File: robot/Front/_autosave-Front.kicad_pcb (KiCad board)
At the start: 2 copper layers, 40 x 40 mm, 42 parts, among them J1 USB_B_Micro, Q1 BC849, Q2 BC849, SW2 SW_Push, U1 CH340C, U10 ESP32-WROOM-32, U2 CJVL53L0XV2, U3 LD1117S33CTR

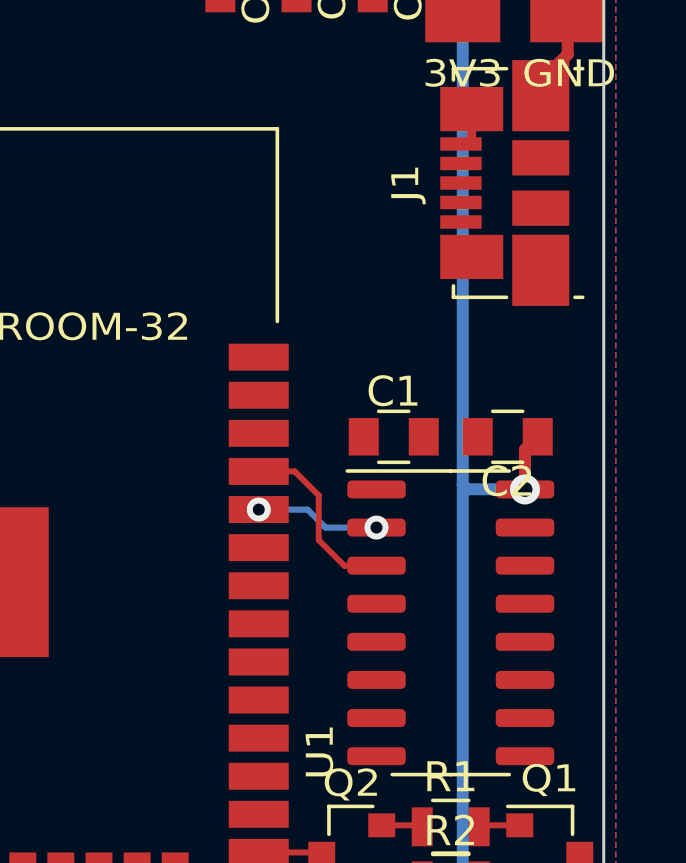
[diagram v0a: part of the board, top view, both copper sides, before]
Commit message: Shrink design
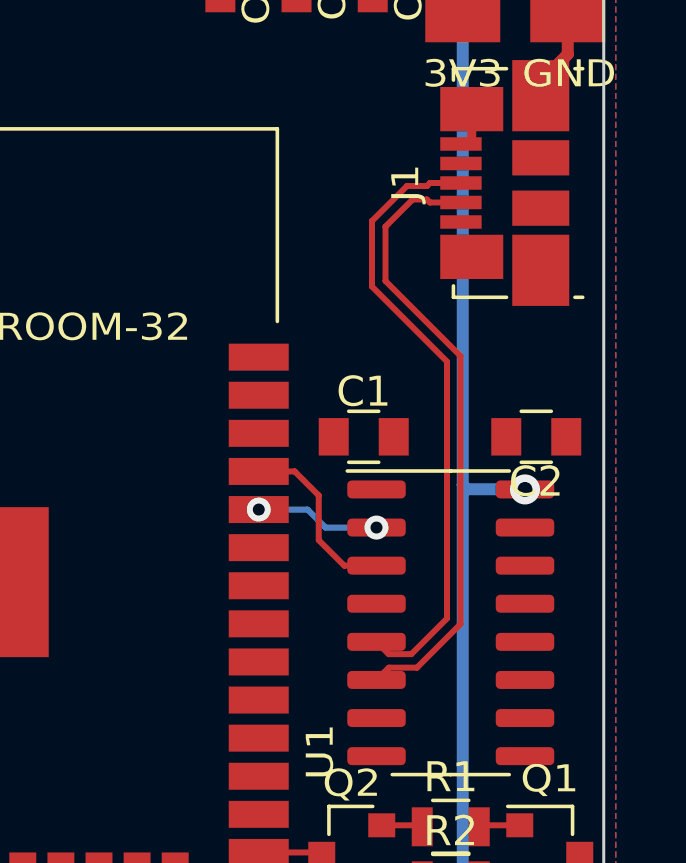
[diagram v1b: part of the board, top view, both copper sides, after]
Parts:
- moved C1 1.00 mm to (227.5, 121.1)
- moved C2 0.95 mm to (233.2, 121.1)
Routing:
- net /D-: track 0.00 -> 20.8 mm
- net /D+: track 0.00 -> 20.8 mm
- net +3V3: track 101.6 -> 99.7 mm
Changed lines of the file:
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@@
     (thickness 1.6)
     (drawings 7)
-    (tracks 131)
+    (tracks 149)
     (zones 0)
     (modules 42)
@@
   )
   (module Capacitors_SMD:C_0805 (layer F.Cu)
-    (at 228.5 121.1)
+    (at 227.5 121.1)
     (descr "Capacitor SMD 0805, reflow soldering, AVX (see smccp.pdf)")
     (tags "capacitor 0805")
@@
   )
   (module Capacitors_SMD:C_0805 (layer F.Cu)
-    (at 232.3 121.1 180)
+    (at 233.25 121.1 180)
     (descr "Capacitor SMD 0805, reflow soldering, AVX (see smccp.pdf)")
     (tags "capacitor 0805")
@@
   (via (at 230.8 140.55) (size 1) (drill 0.5) (layers F.Cu B.Cu) (net 4))
   (via (at 232.875 122.855) (size 1) (drill 0.5) (layers F.Cu B.Cu) (net 4))
-  (segment (start 232.875 121.525) (end 233.3 121.1) (width 0.4) (layer F.Cu) (net 4))
-  (segment (start 232.875 122.855) (end 232.875 121.525) (width 0.4) (layer F.Cu) (net 4))
   (segment (start 230.8 105.45) (end 230.8 122.7) (width 0.4) (layer B.Cu) (net 4))
   (segment (start 230.8 122.7) (end 230.8 140.55) (width 0.4) (layer B.Cu) (net 4))
@@
   (segment (start 204.525 136.88) (end 206.45 134.955) (width 0.4) (layer B.Cu) (net 35))
   (segment (start 201.64 136.88) (end 204.525 136.88) (width 0.4) (layer B.Cu) (net 35))
+  (segment (start 227.925 129.205) (end 228.335 128.795) (width 0.2) (layer F.Cu) (net 36))
+  (segment (start 228.335 128.795) (end 229.2732 128.795) (width 0.2) (layer F.Cu) (net 36))
+  (segment (start 229.2732 128.795) (end 230.725 127.3432) (width 0.2) (layer F.Cu) (net 36))
+  (segment (start 230.725 127.3432) (end 230.725 118.4068) (width 0.2) (layer F.Cu) (net 36))
+  (segment (start 230.725 118.4068) (end 228.225 115.9068) (width 0.2) (layer F.Cu) (net 36))
+  (segment (start 228.225 115.9068) (end 228.225 114.0932) (width 0.2) (layer F.Cu) (net 36))
+  (segment (start 229.704999 113.29) (end 230.74 113.29) (width 0.2) (layer F.Cu) (net 36))
+  (segment (start 229.604999 113.19) (end 229.704999 113.29) (width 0.2) (layer F.Cu) (net 36))
+  (segment (start 228.225 114.0932) (end 229.1282 113.19) (width 0.2) (layer F.Cu) (net 36))
+  (segment (start 229.1282 113.19) (end 229.604999 113.19) (width 0.2) (layer F.Cu) (net 36))
+  (segment (start 227.925 127.935) (end 228.335 128.345) (width 0.2) (layer F.Cu) (net 37))
+  (segment (start 228.335 128.345) (end 229.0868 128.345) (width 0.2) (layer F.Cu) (net 37))
+  (segment (start 229.0868 128.345) (end 230.275 127.1568) (width 0.2) (layer F.Cu) (net 37))
+  (segment (start 230.275 127.1568) (end 230.275 118.5932) (width 0.2) (layer F.Cu) (net 37))
+  (segment (start 230.275 118.5932) (end 227.775 116.0932) (width 0.2) (layer F.Cu) (net 37))
+  (segment (start 227.775 116.0932) (end 227.775 113.9068) (width 0.2) (layer F.Cu) (net 37))
+  (segment (start 228.9418 112.74) (end 229.604999 112.74) (width 0.2) (layer F.Cu) (net 37))
+  (segment (start 227.775 113.9068) (end 228.9418 112.74) (width 0.2) (layer F.Cu) (net 37))
+  (segment (start 229.604999 112.74) (end 229.704999 112.64) (width 0.2) (layer F.Cu) (net 37))
+  (segment (start 229.704999 112.64) (end 230.74 112.64) (width 0.2) (layer F.Cu) (net 37))
   (zone (net 0) (net_name "") (layers F&B.Cu) (hatch edge 0.508)
     (connect_pads (clearance 0.508))
